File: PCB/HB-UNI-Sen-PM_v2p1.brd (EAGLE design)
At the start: 40 x 40.4 mm, 28 parts, among them IC1 MCP1700T-3302E_MB, IC3 MEGA8-AI, Q1 CSTCE, U1 CC1101SMD

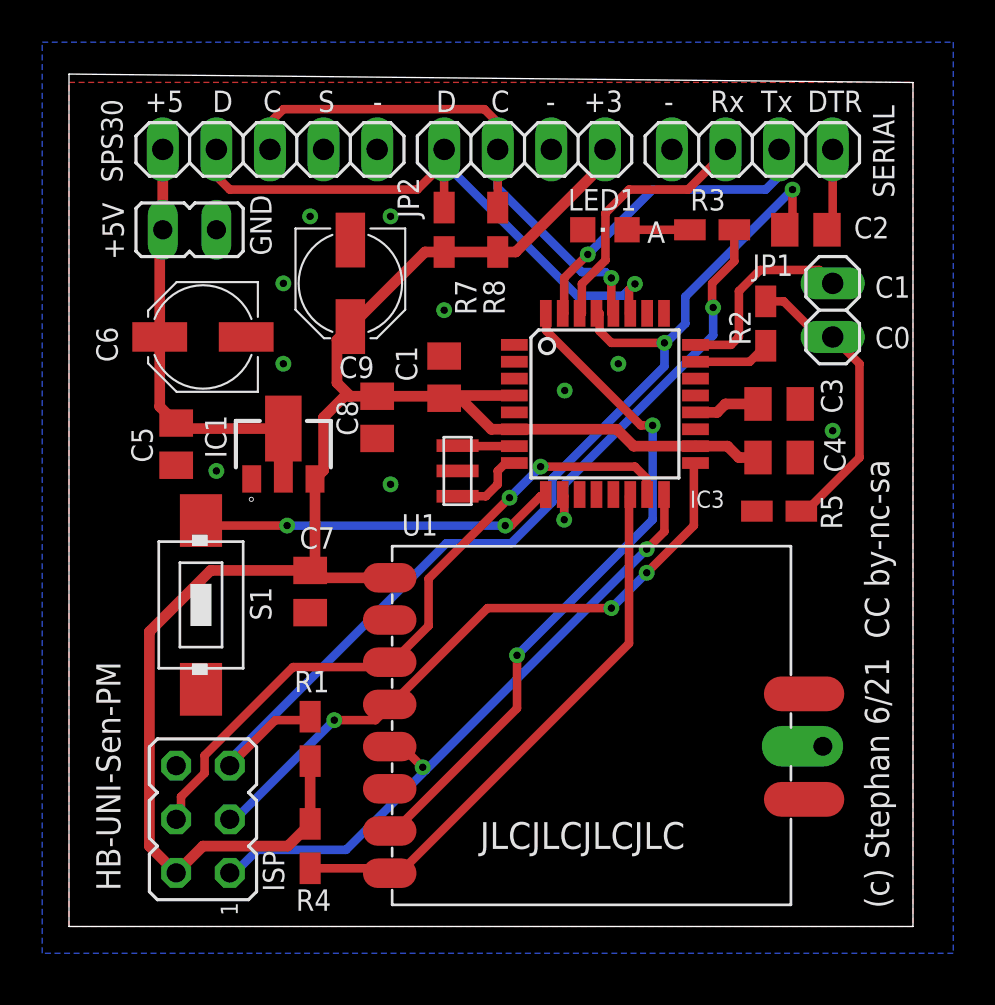
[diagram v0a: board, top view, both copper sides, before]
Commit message: pcb silkscreen corrected in v2.1, first working version of software
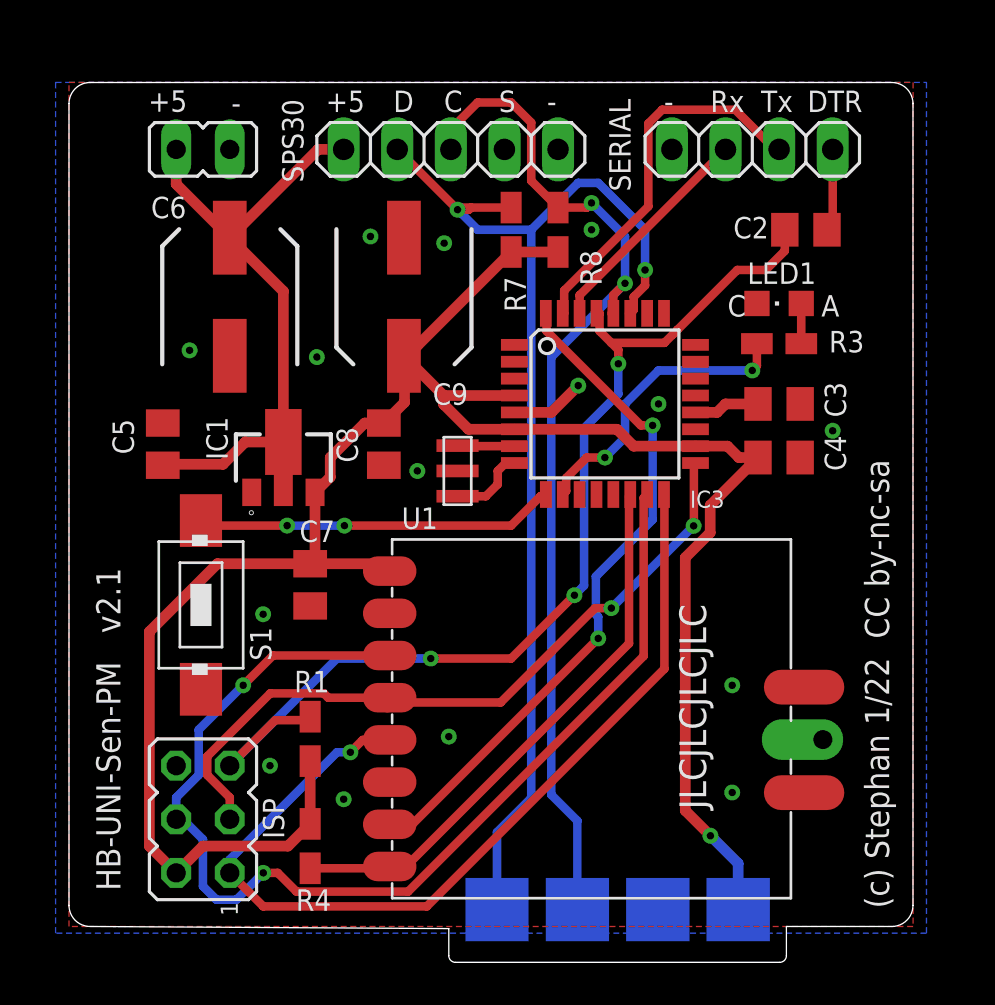
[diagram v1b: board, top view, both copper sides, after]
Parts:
- removed C1: 100n, resistor:C0805K
- removed JP1: IO, pinhead:1X02
- removed JP2: I2C, pinhead:1X04
- removed R2, R5: 10k, resistor:R0805W
- added U$1: LOETKONTAKT4P, StephansLib:LOETKONTAKT4P
- C6, C9: device rcl:PANASONIC_C -> rcl:SANYO-OSCON_SMD_C6
- S1: value SMDSWITCH6X4 -> CONFIG
- moved LED1 8.96 mm to (33.7, 29.5)
- moved SPS30 8.57 mm to (18.1, 36.8)
- moved R3 6.26 mm to (33.7, 27.6), turned to 0 degrees
- moved BATT 3.86 mm to (6.35, 36.8)
- moved R7 3.17 mm to (21.0, 33.0)
- moved R8 2.86 mm to (23.2, 33.0)
- moved C9 2.62 mm to (15.9, 29.8)
- moved C6 2.29 mm to (7.62, 29.8), turned to 90 degrees
- moved C8 1.31 mm to (14.9, 22.9)
- moved C5 0.63 mm to (4.45, 22.9), turned to 90 degrees
- moved IC1 0.63 mm to (10.2, 22.2)
- moved C7 0.32 mm to (11.4, 16.2)
- moved U1 0.32 mm to (24.8, 9.84)
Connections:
- removed net PC0: IC3.23, R2.2
- removed net PC0DIV: JP1.1, R2.1, R5.2
- removed net PC1: IC3.24, JP1.2
- net 3V3: now also U$1.P$4; no longer C1.1, JP2.4
- net GND: now also U$1.P$3; no longer C1.2, JP2.3, R5.1
- net SCL: now also U$1.P$2; no longer JP2.2
- net SDA: now also U$1.P$1; no longer JP2.1
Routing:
- net SDA: track 30.3 -> 55.9 mm, vias 1 -> 2
- net SCL: track 27.4 -> 49.8 mm, vias 1 -> 2
- net MOSI: track 32.5 -> 54.0 mm
- net 3V3: track 87.5 -> 103.1 mm, vias 0 -> 1
- net MISO: track 31.4 -> 45.8 mm, vias 2 -> 1
- net PC0DIV: track 13.9 -> 0.00 mm
- net 5V: track 20.8 -> 31.6 mm
- net PC1: track 9.51 -> 0.00 mm
- net PD6: track 18.6 -> 14.1 mm
- net SCLK: track 30.8 -> 34.9 mm, vias 3 -> 2
- net PC0: track 3.64 -> 0.00 mm
- net GND: track 0.00 -> 3.55 mm, vias 10 -> 15
- net TXD: track 15.2 -> 18.0 mm, vias 1 -> 0
- net RXD: track 12.3 -> 10.6 mm
- net LED1: track 2.98 -> 1.91 mm
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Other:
- board size 40 x 40.4 mm -> 40 x 41.7 mm
- board text added: "(c) Stephan 1/22 CC by-nc-sa"
- board text added: "HB-UNI-Sen-PM v2.1"
- board text removed: "(c) Stephan 6/21 CC by-nc-sa"
- board text removed: "+5V"
- board text removed: "C0"
- board text removed: "C1"
- board text removed: "GND"
- board text removed: "HB-UNI-Sen-PM"
